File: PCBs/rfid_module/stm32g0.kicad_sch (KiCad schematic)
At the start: 5 parts, among them U301 STM32G071G8Ux

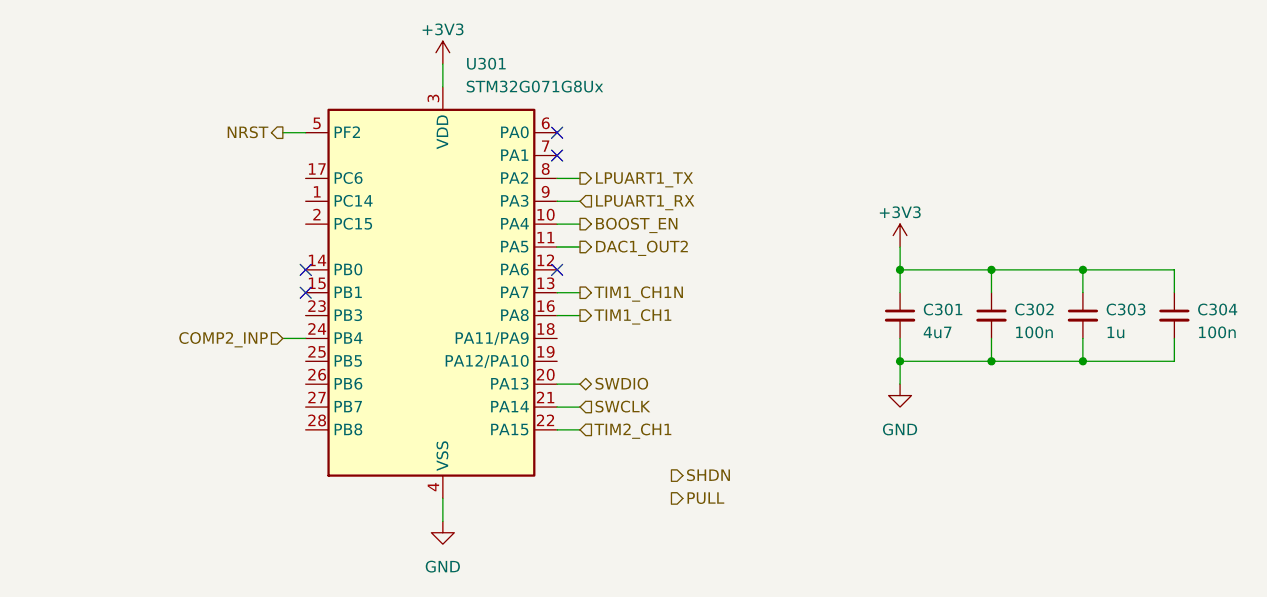
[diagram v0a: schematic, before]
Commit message: RFID PCB Done, started lower flex PCB
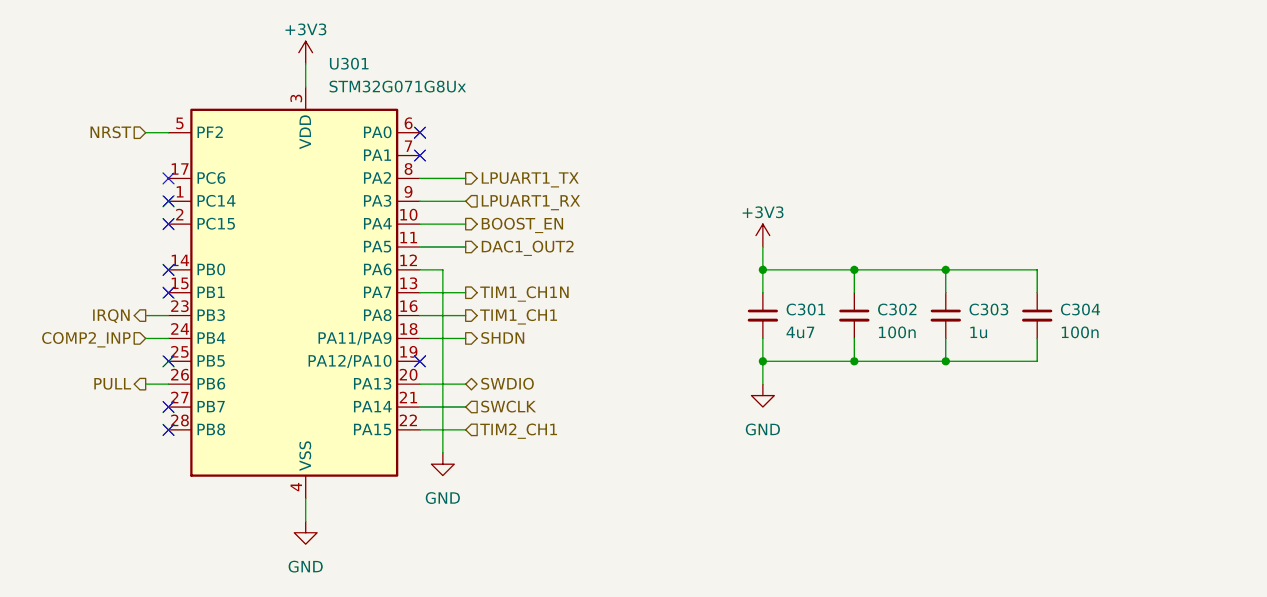
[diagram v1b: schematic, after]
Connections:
- net GND: now also U301.12 (PA6)
- net PULL: now also U301.26 (PB6)
- net SHDN: now also U301.18 (PA11/PA9)
- net IRQN: now reaches U301.23 (PB3)
- no-connect marks 5 -> 11
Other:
- moved on the sheet: C301, C302, C303, C304, U301
